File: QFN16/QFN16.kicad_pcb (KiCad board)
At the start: 2 copper layers, 13 x 20.6 mm, 10 parts, among them J1 Conn_01x08, J2 Conn_02x08_Counter_Clockwise, J3 Conn_01x08, J4 Conn_02x08_Counter_Clockwise

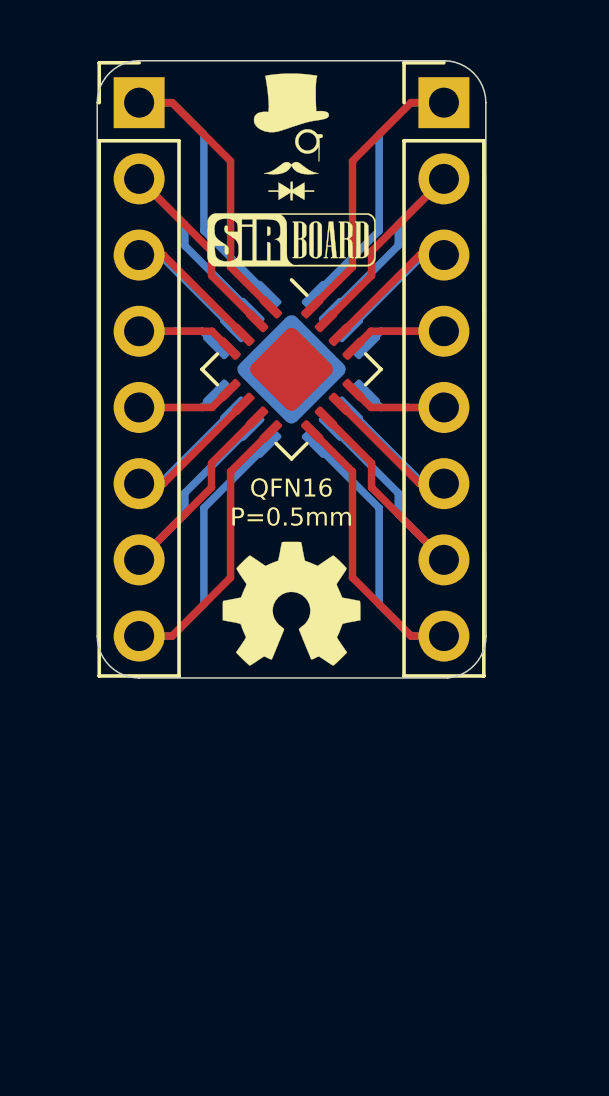
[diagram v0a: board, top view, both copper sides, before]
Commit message: Silkscreens and sizes updated
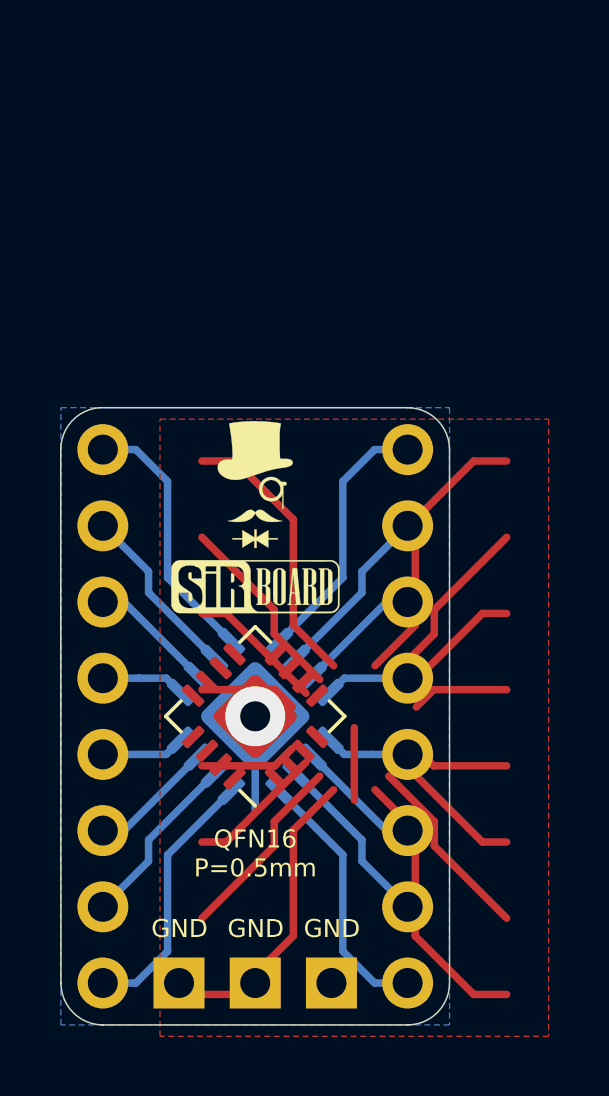
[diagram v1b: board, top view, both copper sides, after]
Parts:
- removed REF** (x2): OSHW-Logo2_7.3x6mm_SilkScreen, Symbol:OSHW-Logo2_7.3x6mm_SilkScreen
- added J5: Conn_01x03, Connector_PinHeader_2.54mm:PinHeader_1x03_P2.54mm_Vertical, B.Cu at (147.6, 115.8)
- moved J3 31.5 mm to (140.0, 115.8), turned to 180 degrees
- moved J1 30.7 mm to (150.2, 115.8), turned to 180 degrees
- moved G*** 11.7 mm to (145.1, 99.2)
- moved J2 11.6 mm to (145.1, 106.9), turned to 135 degrees
- moved J4 11.6 mm to (145.1, 106.9), turned to 225 degrees
- moved G*** 11.6 mm to (145.1, 102.6)
- moved G*** 4.60 mm to (145.1, 98.9), turned to 180 degrees
- moved G*** 2.26 mm to (145.1, 102.1), turned to 180 degrees
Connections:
- J2 pad 17: (no net) -> Net-(J5-Pad1)
- J4 pad 17: (no net) -> Net-(J5-Pad1)
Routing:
- net Net-(J5-Pad1): track 0.00 -> 14.9 mm, vias 0 -> 1
- net Net-(J1-Pad5): track 6.04 -> 17.0 mm
- net Net-(J1-Pad4): track 6.04 -> 17.0 mm
- net Net-(J1-Pad1): track 18.1 -> 8.82 mm
- net Net-(J2-Pad16): track 18.1 -> 8.82 mm
- net Net-(J1-Pad7): track 12.3 -> 5.96 mm
- net Net-(J1-Pad2): track 12.3 -> 5.96 mm
- net Net-(J1-Pad3): track 8.74 -> 13.5 mm
- net Net-(J1-Pad6): track 8.74 -> 4.17 mm
- net Net-(J2-Pad13): track 6.04 -> 2.78 mm
- net Net-(J2-Pad15): track 12.3 -> 15.6 mm
- added copper zone on B.Cu, net Net-(J5-Pad1)
- added copper zone on F.Cu, net Net-(J5-Pad1)
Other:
- outline, holes or cut-outs redrawn
- net class Default: clearance 0.2 -> 0.127; trace_width 0.25 -> 0.127
- rule trace_clearance: 0.2 -> 0.127
- rule trace_min: 0.2 -> 0.127
- rule via_min_size: 0.4 -> 0.3
- board text added: "GND"

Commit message: QFN16 Revised
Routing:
- net Net-(J2-Pad16): track 8.82 -> 8.17 mm
- net Net-(J1-Pad1): track 8.82 -> 8.17 mm
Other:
- board size 13 x 20.6 mm -> 16.4 x 23 mm
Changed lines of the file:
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@@
   (page A4)
   (layers
-    (0 F.Cu signal hide)
+    (0 F.Cu signal)
     (31 B.Cu signal)
     (32 B.Adhes user hide)
@@
   )
   (setup
-    (last_trace_width 0.127)
+    (last_trace_width 0.25)
     (user_trace_width 0.2)
     (user_trace_width 0.25)
@@
   (gr_arc (start 140.014 98.052) (end 139.887001 96.655001) (angle -84.80557109) (layer Edge.Cuts) (width 0.05))
   (gr_arc (start 150.174 98.052) (end 151.571 98.052) (angle -90) (layer Edge.Cuts) (width 0.05))
-  (gr_arc (start 150.174 115.832) (end 150.174 117.229) (angle -90) (layer Edge.Cuts) (width 0.05))
-  (gr_arc (start 140.014 115.832) (end 138.617 115.832) (angle -90) (layer Edge.Cuts) (width 0.05))
+  (gr_arc (start 150.876 118.237) (end 150.876 119.634) (angle -90) (layer Edge.Cuts) (width 0.05))
+  (gr_arc (start 137.287 116.84) (end 135.89 116.84) (angle -90) (layer Edge.Cuts) (width 0.05))
   (segment (start 150.428 103.912142) (end 150.428 100.381) (width 0.25) (layer F.Cu) (net 1))
   (segment (start 150.428 100.381) (end 152.376 98.433) (width 0.25) (layer F.Cu) (net 1))
@@
   (segment (start 148.65 111.768) (end 150.174 113.292) (width 0.25) (layer B.Cu) (net 7))
   (segment (start 148.65 111.063685) (end 148.65 111.768) (width 0.25) (layer B.Cu) (net 7))
-  (segment (start 145.889495 109.434551) (end 148.015 111.560056) (width 0.25) (layer B.Cu) (net 8))
-  (segment (start 149.074 115.832) (end 150.174 115.832) (width 0.25) (layer B.Cu) (net 8))
-  (segment (start 148.015 114.773) (end 149.074 115.832) (width 0.25) (layer B.Cu) (net 8))
-  (segment (start 148.015 111.560056) (end 148.015 114.773) (width 0.25) (layer B.Cu) (net 8))
-  (segment (start 142.173 114.773) (end 141.114 115.832) (width 0.25) (layer B.Cu) (net 9))
-  (segment (start 144.298505 109.434551) (end 142.173 111.560056) (width 0.25) (layer B.Cu) (net 9))
-  (segment (start 142.173 111.560056) (end 142.173 114.773) (width 0.25) (layer B.Cu) (net 9))
-  (segment (start 141.114 115.832) (end 140.014 115.832) (width 0.25) (layer B.Cu) (net 9))
+  (segment (start 148.015 111.560056) (end 145.889495 109.434551) (width 0.25) (layer B.Cu) (net 8))
+  (segment (start 148.015 113.217) (end 148.015 111.560056) (width 0.25) (layer B.Cu) (net 8))
+  (segment (start 150.174 115.832) (end 150.174 115.376) (width 0.25) (layer B.Cu) (net 8))
+  (segment (start 150.174 115.376) (end 148.015 113.217) (width 0.25) (layer B.Cu) (net 8))
+  (segment (start 142.173 111.560056) (end 144.298505 109.434551) (width 0.25) (layer B.Cu) (net 9))
+  (segment (start 142.173 113.351) (end 142.173 111.560056) (width 0.25) (layer B.Cu) (net 9))
+  (segment (start 140.014 115.832) (end 140.014 115.51) (width 0.25) (layer B.Cu) (net 9))
+  (segment (start 140.014 115.51) (end 142.173 113.351) (width 0.25) (layer B.Cu) (net 9))
   (segment (start 141.538 111.768) (end 140.014 113.292) (width 0.25) (layer B.Cu) (net 10))
   (segment (start 141.538 111.063685) (end 141.538 111.768) (width 0.25) (layer B.Cu) (net 10))

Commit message: QFN16 Copper Pour Revised
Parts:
- moved G*** 27.0 mm to (118.3, 106.2)
- moved G*** 27.0 mm to (118.3, 102.8)
- moved J1 27.0 mm to (123.4, 119.4)
- moved J3 27.0 mm to (113.2, 119.4)
- moved J2 27.0 mm to (118.3, 110.5)
- moved J4 27.0 mm to (118.3, 110.5)
- moved G*** 27.0 mm to (118.3, 105.7)
- moved G*** 27.0 mm to (118.3, 102.5)
- moved J5 27.0 mm to (120.8, 119.4)
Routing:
- net Net-(J1-Pad5): track 17.0 -> 6.04 mm
- net Net-(J1-Pad4): track 17.0 -> 6.04 mm
- net Net-(J5-Pad1): track 14.9 -> 5.59 mm
- net Net-(J1-Pad1): track 8.17 -> 16.1 mm
- net Net-(J2-Pad16): track 8.17 -> 16.1 mm
- net Net-(J1-Pad7): track 5.96 -> 12.3 mm
- net Net-(J1-Pad2): track 5.96 -> 12.3 mm
- net Net-(J1-Pad3): track 13.5 -> 8.74 mm
- net Net-(J1-Pad6): track 4.17 -> 8.74 mm
- net Net-(J2-Pad13): track 2.78 -> 6.04 mm
- net Net-(J2-Pad15): track 15.6 -> 12.3 mm
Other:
- board size 16.4 x 23 mm -> 13 x 20.6 mm

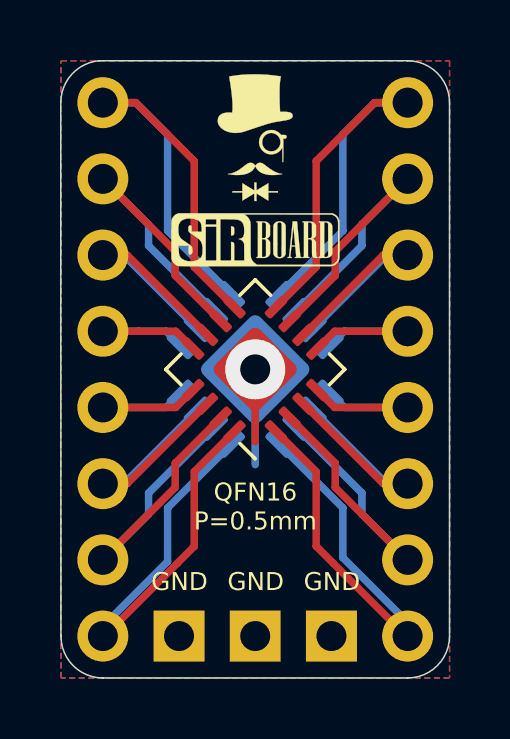
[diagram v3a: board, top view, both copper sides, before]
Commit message: Dimensions Added And TQFP64 Added
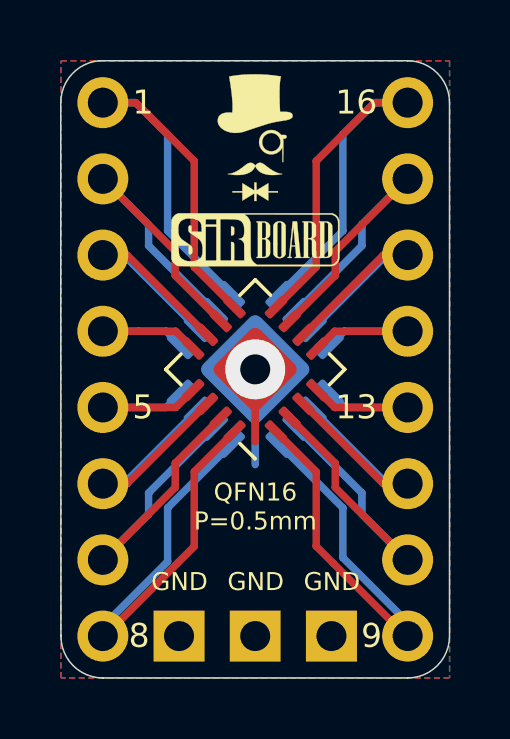
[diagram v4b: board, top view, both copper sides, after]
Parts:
- J1, J3: moved to B.Cu
- turned J1 to 0 degrees
- turned J3 to 0 degrees
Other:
- board text added: "1"
- board text added: "13"
- board text added: "16"
- board text added: "5"
- board text added: "8"
- board text added: "9"

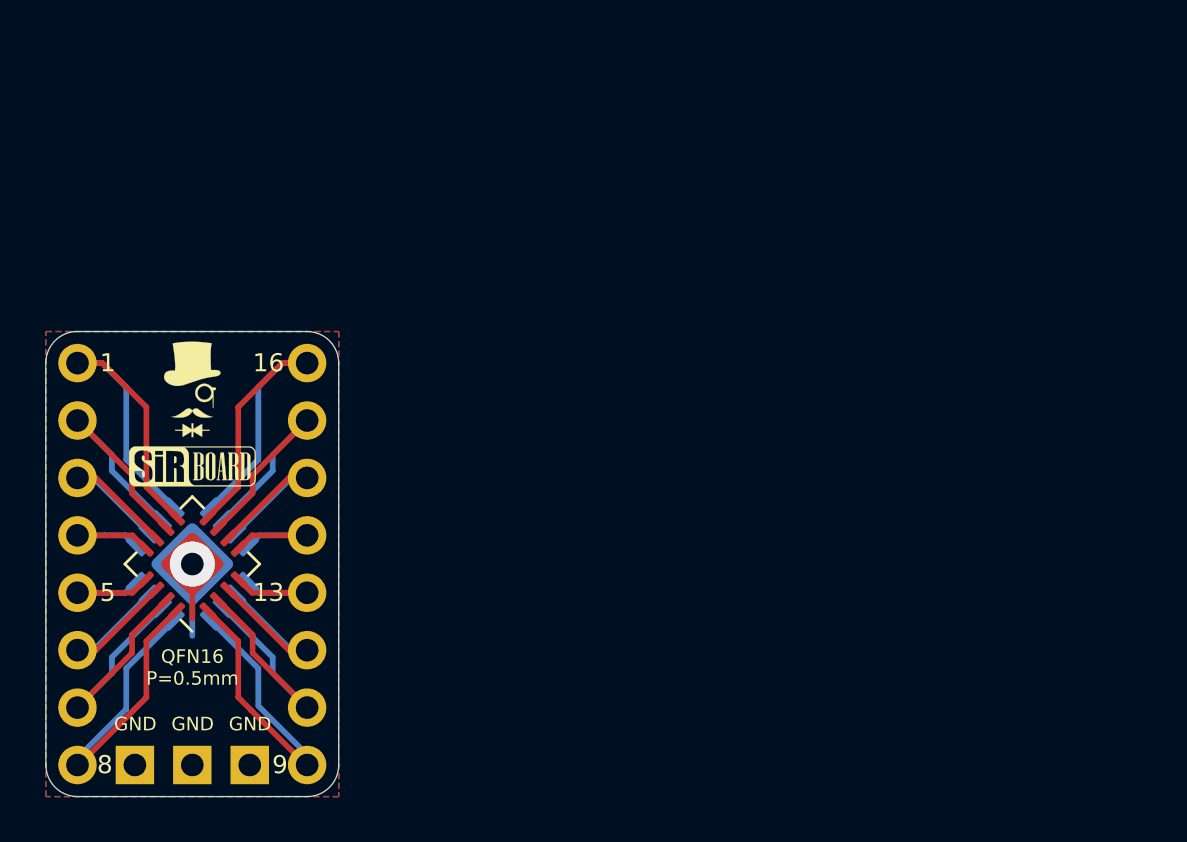
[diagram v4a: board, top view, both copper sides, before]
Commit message: Numbering Orientation Edited
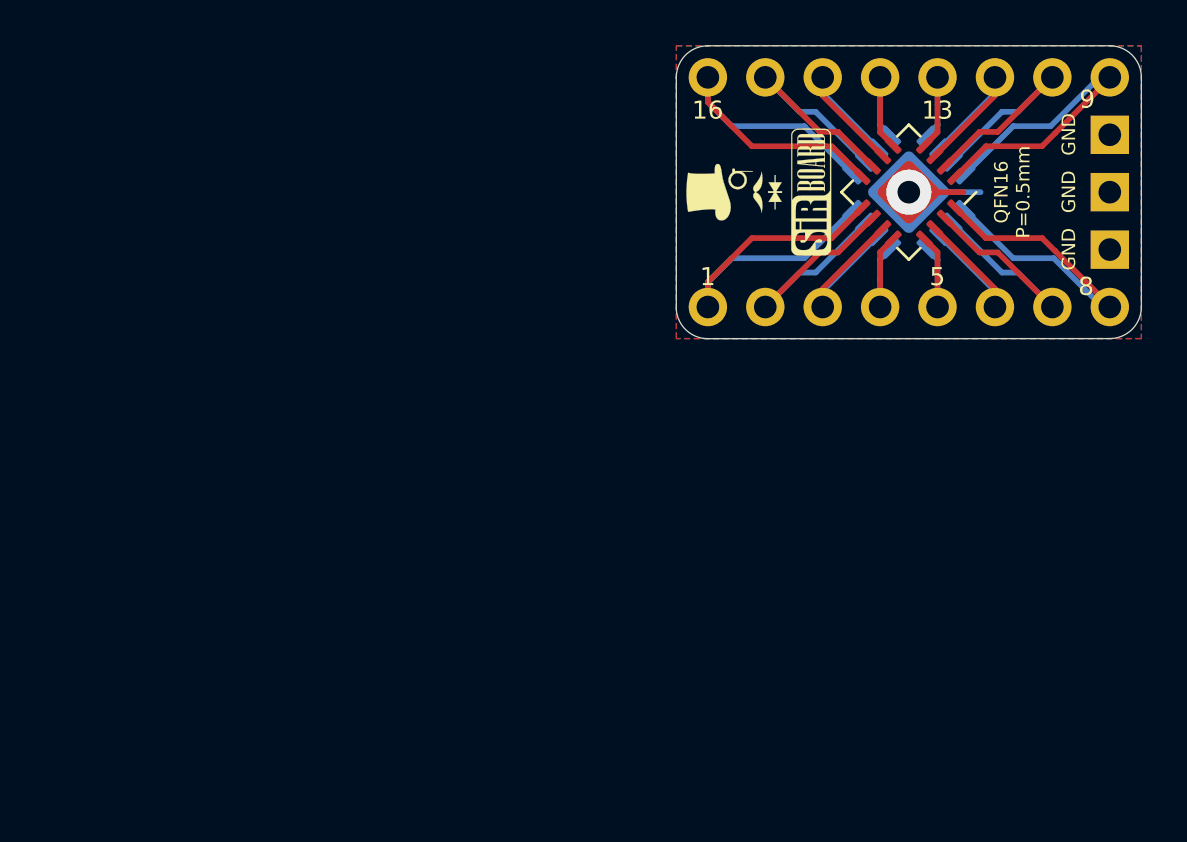
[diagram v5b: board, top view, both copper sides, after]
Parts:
- J1, J3: moved to F.Cu
- moved J3 50.0 mm to (158.9, 99.1), turned to 270 degrees
- moved J5 47.2 mm to (158.9, 91.5), turned to 180 degrees
- moved J1 46.8 mm to (158.9, 89.0), turned to 270 degrees
- moved J2 35.7 mm to (150.0, 94.0), turned to 225 degrees
- moved J4 35.7 mm to (150.0, 94.0), turned to 315 degrees
- moved G*** 29.9 mm to (145.7, 94.0), turned to 90 degrees
- moved G*** 29.3 mm to (145.2, 94.0), turned to 270 degrees
- moved G*** 25.5 mm to (142.3, 94.0), turned to 90 degrees
- moved G*** 25.2 mm to (142.0, 94.0), turned to 270 degrees
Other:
- board size 13 x 20.6 mm -> 20.6 x 13 mm

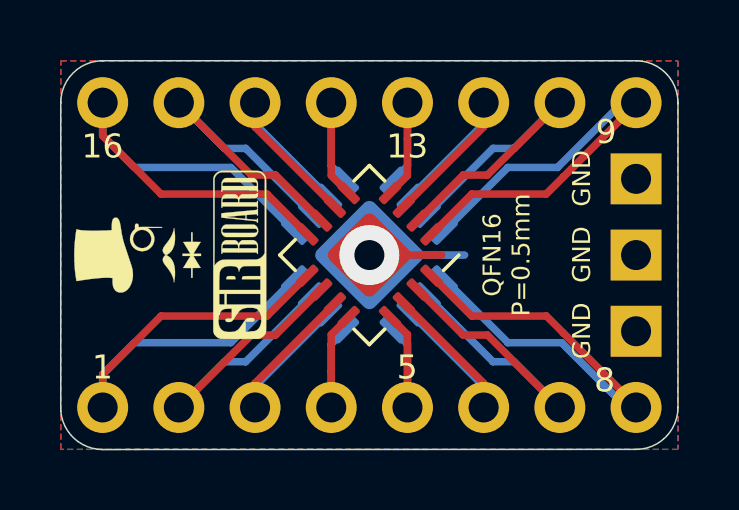
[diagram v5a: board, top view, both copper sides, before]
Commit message: Silkscreen Edits
Dimensions moved to Drawings Layer
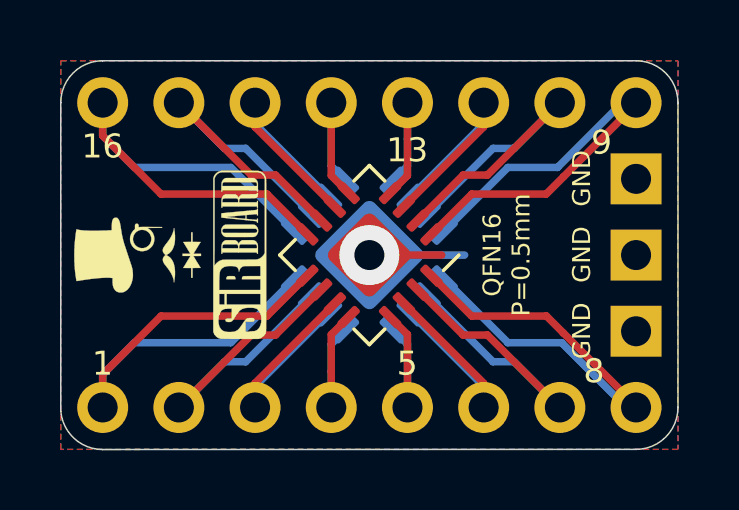
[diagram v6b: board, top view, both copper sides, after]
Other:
- rule pad_to_mask_clearance: 0.051 -> 0
- rule solder_mask_min_width: 0.25 -> 0.1
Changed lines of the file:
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@@
     (pad_size 1.7 1.7)
     (pad_drill 1)
-    (pad_to_mask_clearance 0.051)
-    (solder_mask_min_width 0.25)
+    (pad_to_mask_clearance 0)
+    (solder_mask_min_width 0.1)
     (aux_axis_origin 0 0)
     (visible_elements 7FFFFFFF)
     (pcbplotparams
-      (layerselection 0x010fc_ffffffff)
+      (layerselection 0x010f0_ffffffff)
       (usegerberextensions false)
       (usegerberattributes false)
@@
       (linewidth 0.100000)
       (plotframeref false)
-      (viasonmask false)
+      (viasonmask true)
       (mode 1)
-      (useauxorigin false)
+      (useauxorigin true)
       (hpglpennumber 1)
       (hpglpenspeed 20)
@@
       (psa4output false)
       (plotreference true)
-      (plotvalue true)
+      (plotvalue false)
       (plotinvisibletext false)
       (padsonsilk false)
@@
       (outputformat 1)
       (mirror false)
-      (drillshape 1)
+      (drillshape 0)
       (scaleselection 1)
-      (outputdirectory ""))
+      (outputdirectory "../../Gerbers/QFN16/"))
   )
   (net 0 "")
@@
       (xy -0.033867 1.495778) (xy 0.039511 1.495778) (xy 0.039511 1.626071)) (layer F.SilkS) (width 0.01))
   )
-  (dimension 20.574 (width 0.15) (layer F.SilkS)
-    (gr_text "20.574 mm" (at 149.99462 80.742) (layer F.SilkS)
+  (dimension 20.574 (width 0.15) (layer Dwgs.User)
+    (gr_text "20.574 mm" (at 149.99462 80.742) (layer Dwgs.User)
       (effects (font (size 1 1) (thickness 0.15)) hide)
     )
@@
     (arrow2b (pts (xy 139.70762 82.042) (xy 140.834124 81.455579)))
   )
-  (dimension 17.78 (width 0.15) (layer F.SilkS)
-    (gr_text "17.780 mm" (at 149.995 83.79) (layer F.SilkS)
+  (dimension 17.78 (width 0.15) (layer Dwgs.User)
+    (gr_text "17.780 mm" (at 149.995 83.79) (layer Dwgs.User)
       (effects (font (size 1 1) (thickness 0.15)) hide)
     )
@@
     (arrow2b (pts (xy 141.105 85.09) (xy 142.231504 84.503579)))
   )
-  (dimension 10.16 (width 0.15) (layer F.SilkS)
-    (gr_text "10.160 mm" (at 137.003 94.047 90) (layer F.SilkS)
+  (dimension 10.16 (width 0.15) (layer Dwgs.User)
+    (gr_text "10.160 mm" (at 137.003 94.047 90) (layer Dwgs.User)
       (effects (font (size 1 1) (thickness 0.15)) hide)
     )
@@
     (arrow2b (pts (xy 138.303 99.127) (xy 137.716579 98.000496)))
   )
-  (gr_text 13 (at 151.257 97.663 180) (layer B.SilkS)
+  (gr_text 13 (at 151.257 97.536 180) (layer B.SilkS)
     (effects (font (size 0.8 0.8) (thickness 0.13)) (justify mirror))
   )
@@
     (effects (font (size 0.8 0.8) (thickness 0.13)) (justify mirror))
   )
-  (gr_text 16 (at 141.097 97.409 180) (layer B.SilkS)
+  (gr_text 16 (at 141.097 97.663 180) (layer B.SilkS)
     (effects (font (size 0.8 0.8) (thickness 0.13)) (justify mirror))
   )
-  (gr_text 5 (at 151.257 90.551 180) (layer B.SilkS)
+  (gr_text 5 (at 151.257 90.424 180) (layer B.SilkS)
     (effects (font (size 0.8 0.8) (thickness 0.13)) (justify mirror))
   )
-  (gr_text 1 (at 141.097 90.551 180) (layer B.SilkS)
+  (gr_text 1 (at 141.097 90.424 180) (layer B.SilkS)
     (effects (font (size 0.8 0.8) (thickness 0.13)) (justify mirror))
   )
-  (gr_text 9 (at 157.8864 89.9414) (layer F.SilkS)
+  (gr_text 9 (at 157.734 90.297) (layer F.SilkS)
     (effects (font (size 0.8 0.8) (thickness 0.13)))
   )
-  (gr_text 8 (at 157.8356 98.2218) (layer F.SilkS)
+  (gr_text 8 (at 157.48 97.917) (layer F.SilkS)
     (effects (font (size 0.8 0.8) (thickness 0.13)))
   )
@@
     (effects (font (size 0.8 0.8) (thickness 0.13)))
   )
-  (gr_text 13 (at 151.257 90.424) (layer F.SilkS)
+  (gr_text 13 (at 151.257 90.551) (layer F.SilkS)
     (effects (font (size 0.8 0.8) (thickness 0.13)))
   )
-  (gr_text 5 (at 151.257 97.79) (layer F.SilkS)
+  (gr_text 5 (at 151.257 97.663) (layer F.SilkS)
     (effects (font (size 0.8 0.8) (thickness 0.13)))
   )
-  (gr_text 1 (at 141.097 97.79) (layer F.SilkS)
+  (gr_text 1 (at 141.097 97.663) (layer F.SilkS)
     (effects (font (size 0.8 0.8) (thickness 0.13)))
   )
   (gr_circle (center 149.987 94.0442) (end 149.987 93.2942) (layer F.Mask) (width 0.5))
   (gr_circle (center 149.987 94.0308) (end 149.987 93.2808) (layer B.Mask) (width 0.5))
-  (dimension 12.954 (width 0.15) (layer F.SilkS)
-    (gr_text "12.954 mm" (at 134.147903 94.04604 90) (layer F.SilkS)
+  (dimension 12.954 (width 0.15) (layer Dwgs.User)
+    (gr_text "12.954 mm" (at 134.147903 94.04604 90) (layer Dwgs.User)
       (effects (font (size 1 1) (thickness 0.15)) hide)
     )

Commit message: Page Settings Updated
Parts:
- moved G*** 95.7 mm to (65.5, 41.0)
- moved J2 95.7 mm to (70.4, 41.0)
- moved J4 95.7 mm to (70.4, 41.0)
- moved G*** 95.7 mm to (62.4, 41.0)
- moved G*** 95.7 mm to (66.0, 41.0)
- moved G*** 95.7 mm to (62.6, 41.0)
- moved J1 95.7 mm to (79.3, 35.9)
- moved J3 95.7 mm to (79.3, 46.0)
- moved J5 95.7 mm to (79.3, 38.4)
